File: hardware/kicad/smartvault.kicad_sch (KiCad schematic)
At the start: 0 parts

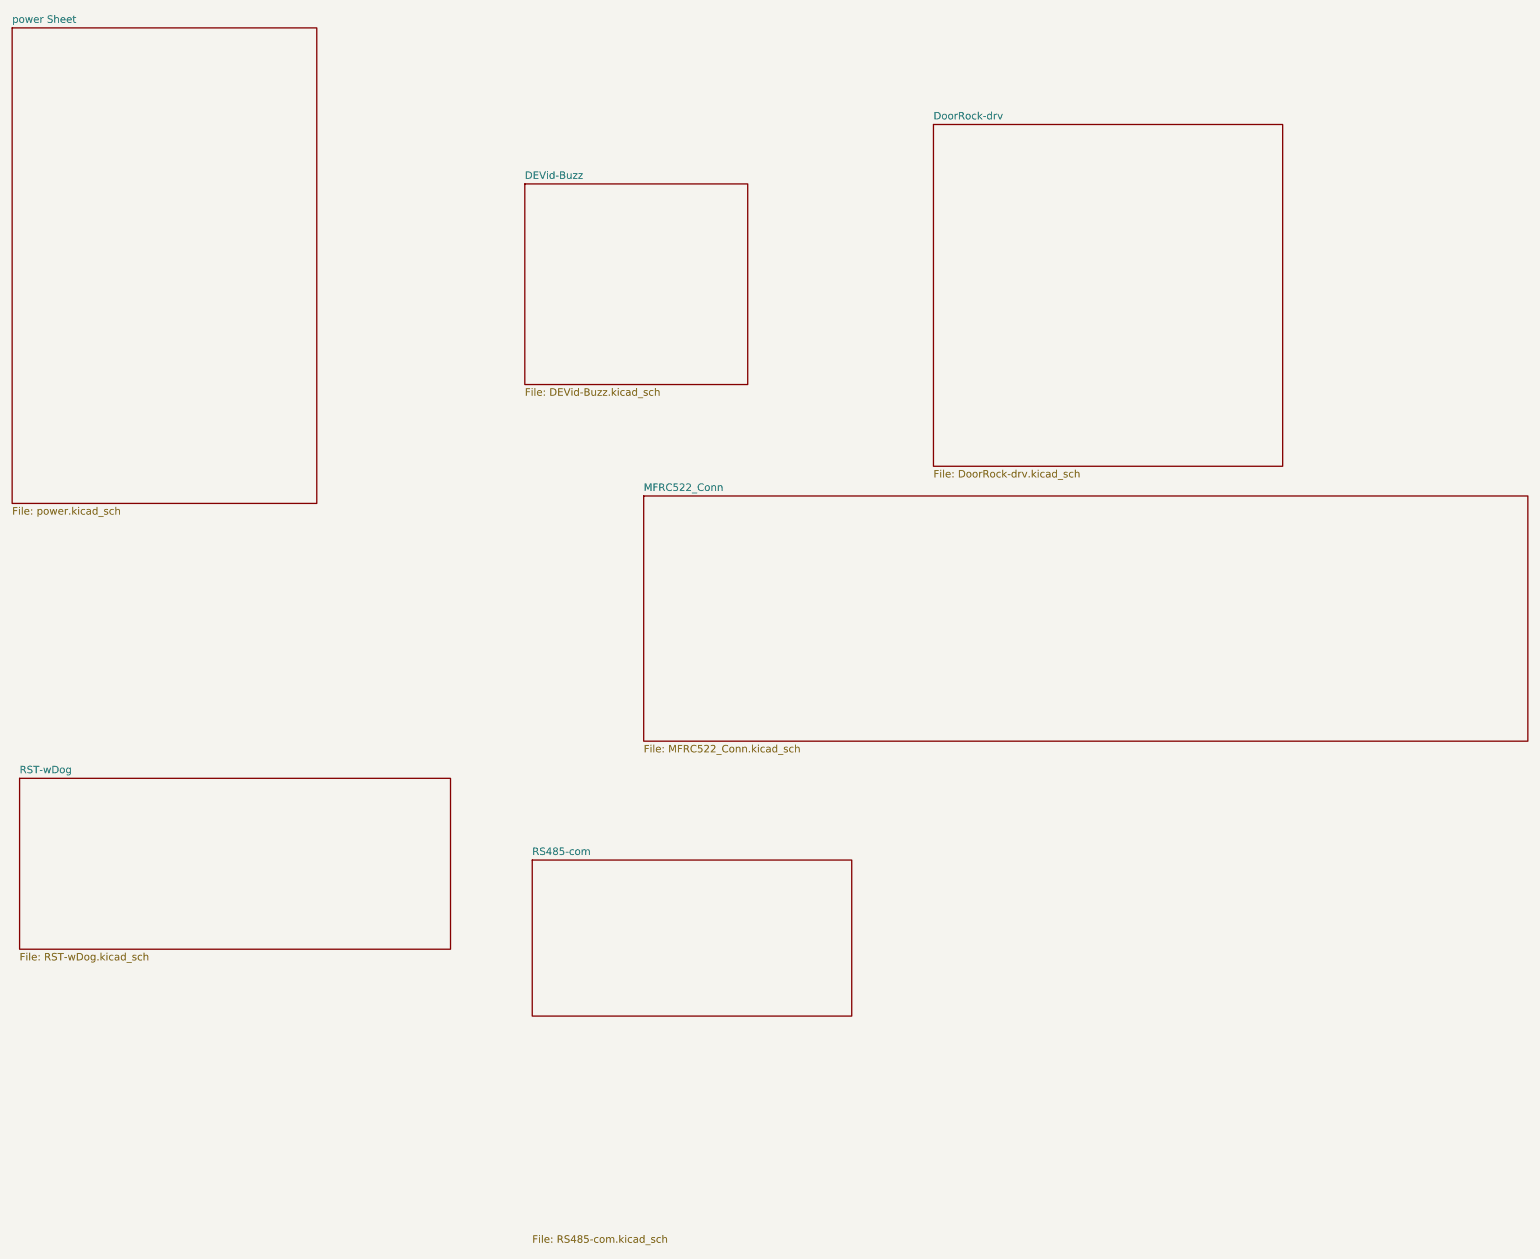
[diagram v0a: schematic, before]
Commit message: chore: KiCad 회로도 최신 변경사항 반영
원본 작업 폴더가 "회로도 편집 완료/20260901_ver01"로 재구성됨(이전 smartvault-pcb-1
경로는 더 이상 존재하지 않음). 하위 시트 6개 전부와 최상위 시트에 실제 설계 변경
있음(DoorRock-drv는 축소, 최상위 시트는 대폭 확장 — 회로가 재구성된 것으로 보임).
PCB 레이아웃 자체는 변경 없음. footprint.xlsx(부품-풋프린트 매핑) 신규 추가.

파일 내부의 프로젝트명 자기참조는 원본 작업 파일명("20260901_ver01")이 아니라
저장소 표준 이름("smartvault")으로 맞춰서 복사 — 작업 폴더 쪽 날짜/버전 파일명
관례를 저장소까지 끌고 오지 않음(git이 버전을 관리).

s_vault.kicad_sym(커스텀 심볼 라이브러리)은 원본 경로에서 찾지 못해 갱신 못함 —
RS485-com/power 시트가 이 라이브러리를 참조하므로, 최신 심볼이 바뀌었다면 다음에
갱신 필요(hardware/README.md에 기록해둠).

Co-Authored-By: Claude Sonnet 5 <noreply@anthropic.com>
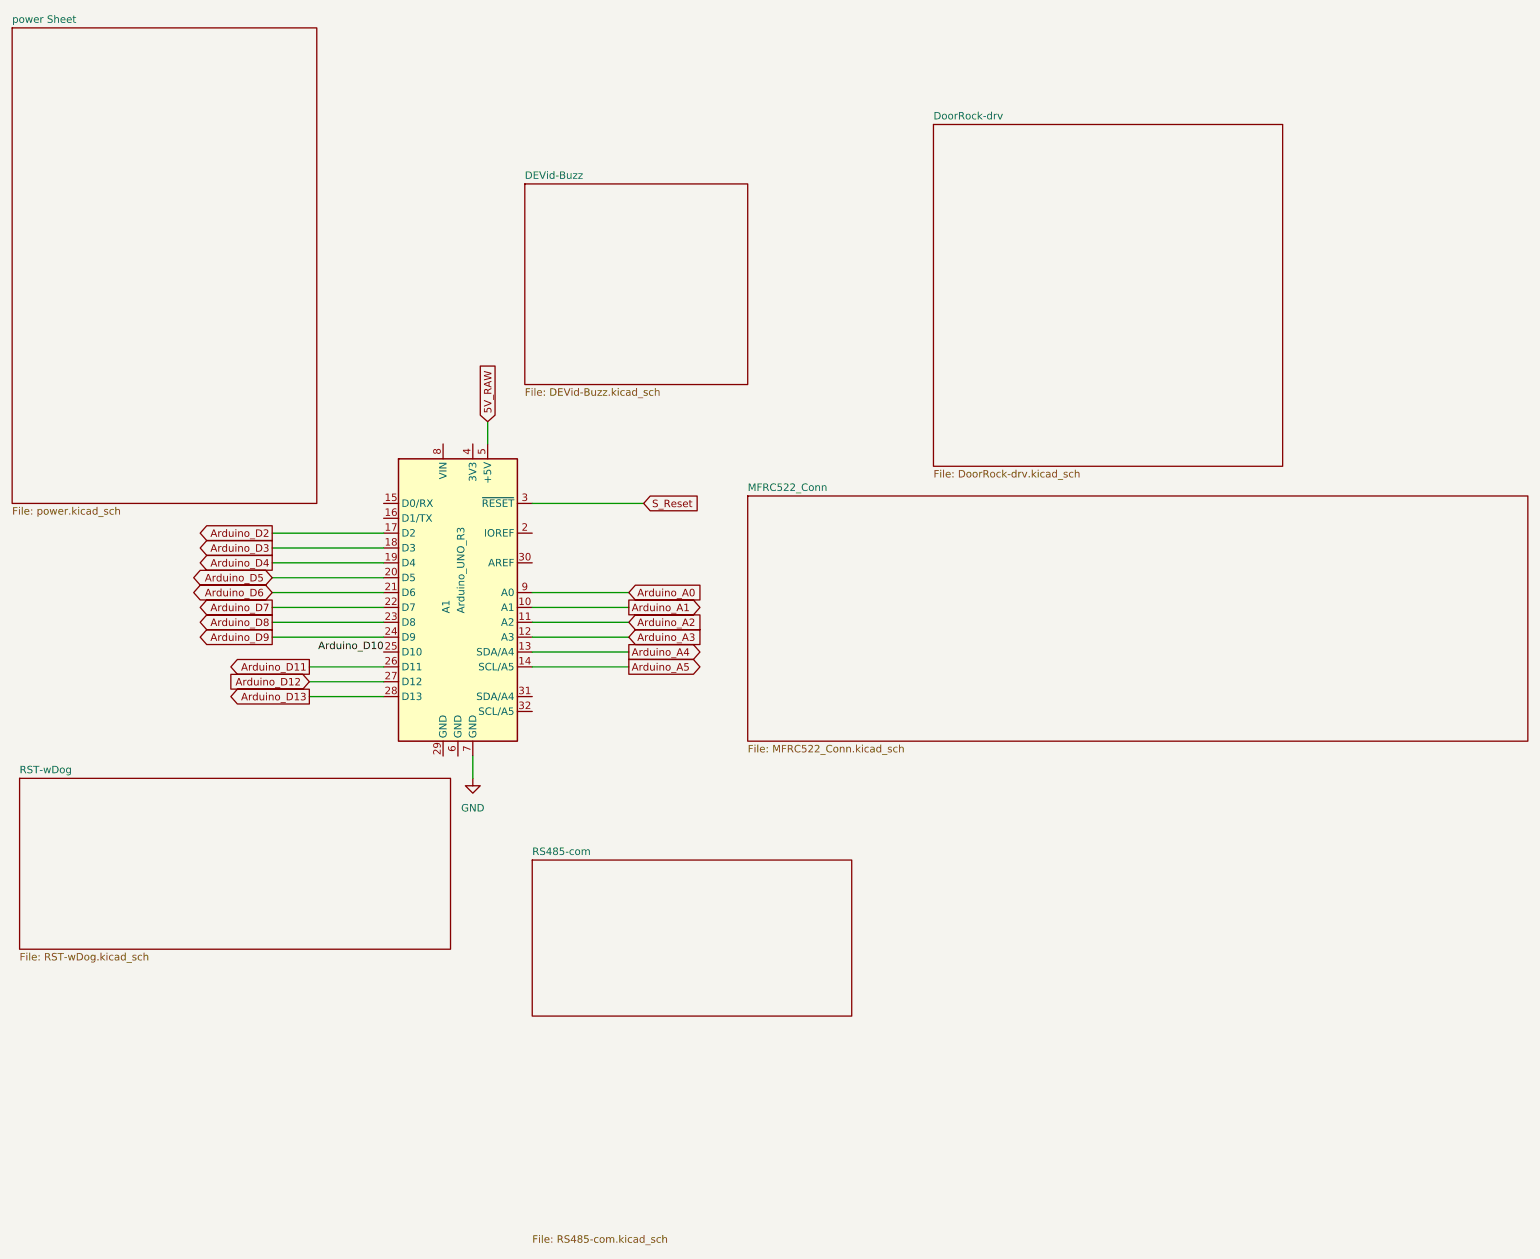
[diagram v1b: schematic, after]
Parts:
- added A1: Arduino_UNO_R3, Module:Arduino_UNO_R3, symbol MCU_Module:Arduino_UNO_R3
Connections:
- new net 5V_RAW: A1.5 (+5V)
- new net Arduino_A0: A1.9 (A0)
- new net Arduino_A1: A1.10 (A1)
- new net Arduino_A2: A1.11 (A2)
- new net Arduino_A3: A1.12 (A3)
- new net Arduino_A4: A1.13 (SDA/A4)
- new net Arduino_A5: A1.14 (SCL/A5)
- new net Arduino_D10: A1.25 (D10)
- new net Arduino_D11: A1.26 (D11)
- new net Arduino_D12: A1.27 (D12)
- new net Arduino_D13: A1.28 (D13)
- new net Arduino_D2: A1.17 (D2)
- new net Arduino_D3: A1.18 (D3)
- new net Arduino_D4: A1.19 (D4)
- new net Arduino_D5: A1.20 (D5)
- new net Arduino_D6: A1.21 (D6)
- new net Arduino_D7: A1.22 (D7)
- new net Arduino_D8: A1.23 (D8)
- new net Arduino_D9: A1.24 (D9)
- new net GND: A1.7 (GND)
- new net S_Reset: A1.3 (~{RESET})
